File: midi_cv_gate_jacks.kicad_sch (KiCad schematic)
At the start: 32 parts, among them J10 CV_I, J11 CV_J, J12 CV_K, J13 CV_L, J14 CV_M, J15 CV_N, J16 CV_O, J17 CV_P, J18 GATE_A, J19 GATE_B, J2 CV_A, J20 GATE_C, J21 GATE_D, J22 GATE_E, J23 GATE_F, J24 GATE_G, J25 GATE_H, J26 GATE_I, J27 GATE_J, J28 GATE_K, J29 GATE_L, J3 CV_B, J30 GATE_M, J31 GATE_N, J32 GATE_O, J33 GATE_P, J4 CV_C, J5 CV_D, J6 CV_E, J7 CV_F, J8 CV_G, J9 CV_H

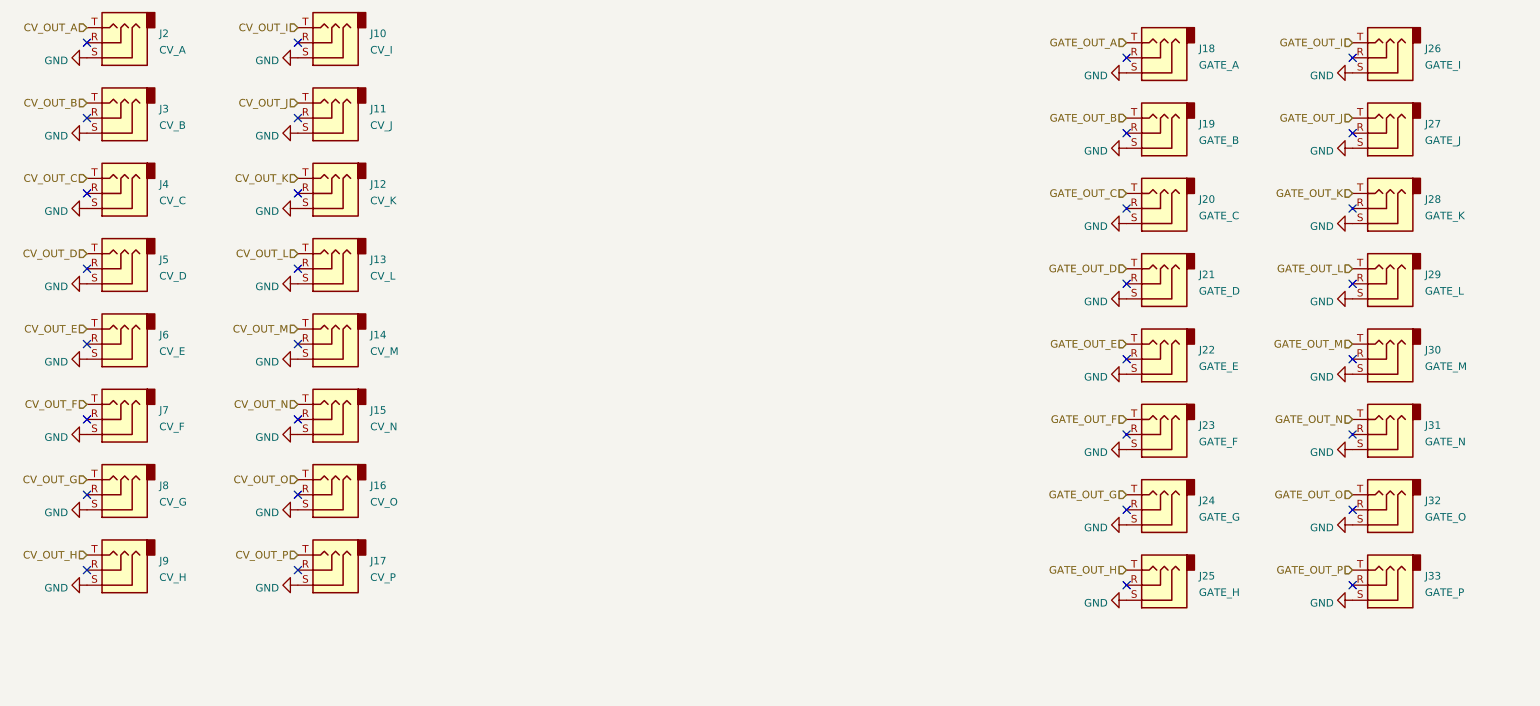
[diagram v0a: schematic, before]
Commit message: Replace soic-14 with dip 14 for DACs, add pulldowns on opamp inputs
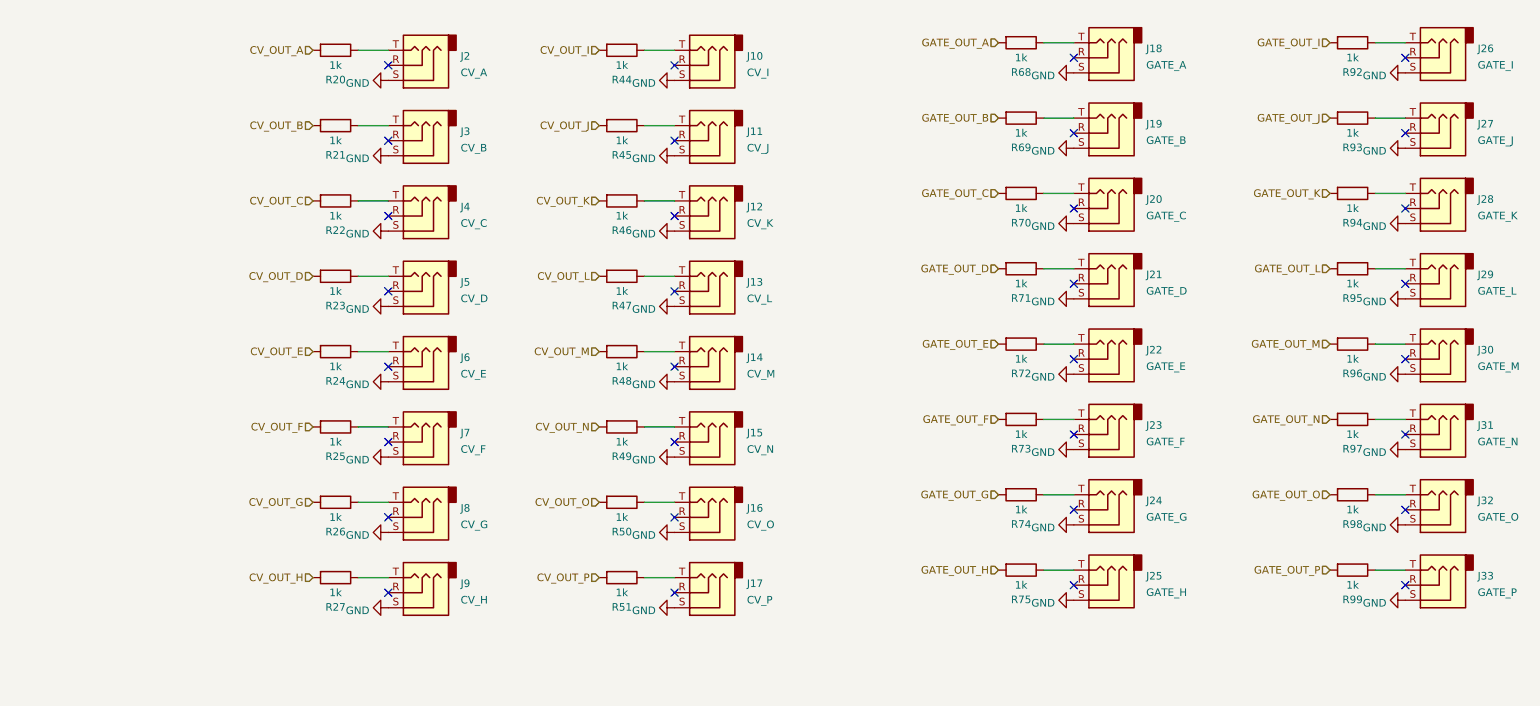
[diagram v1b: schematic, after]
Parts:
- added R20, R21, R22, R23, R24, R25, R26, R27, R44, R45, R46, R47, R48, R49, R50, R51, R68, R69, R70, R71, R72, R73, R74, R75, R92, R93, R94, R95, R96, R97, R98, R99: 1k, Resistor_SMD:R_1206_3216Metric_Pad1.30x1.75mm_HandSolder, symbol Device:R
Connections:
- net CV_OUT_A: now also R20.2; no longer J2.T
- net CV_OUT_B: now also R21.2; no longer J3.T
- net CV_OUT_C: now also R22.2; no longer J4.T
- net CV_OUT_D: now also R23.2; no longer J5.T
- net CV_OUT_E: now also R24.2; no longer J6.T
- net CV_OUT_F: now also R25.2; no longer J7.T
- net CV_OUT_G: now also R26.2; no longer J8.T
- net CV_OUT_H: now also R27.2; no longer J9.T
- net CV_OUT_I: now also R44.2; no longer J10.T
- net CV_OUT_J: now also R45.2; no longer J11.T
- net CV_OUT_K: now also R46.2; no longer J12.T
- net CV_OUT_L: now also R47.2; no longer J13.T
- net CV_OUT_M: now also R48.2; no longer J14.T
- net CV_OUT_N: now also R49.2; no longer J15.T
- net CV_OUT_O: now also R50.2; no longer J16.T
- net CV_OUT_P: now also R51.2; no longer J17.T
- net GATE_OUT_A: now also R68.2; no longer J18.T
- net GATE_OUT_B: now also R69.2; no longer J19.T
- net GATE_OUT_C: now also R70.2; no longer J20.T
- net GATE_OUT_D: now also R71.2; no longer J21.T
- net GATE_OUT_E: now also R72.2; no longer J22.T
- net GATE_OUT_F: now also R73.2; no longer J23.T
- net GATE_OUT_G: now also R74.2; no longer J24.T
- net GATE_OUT_H: now also R75.2; no longer J25.T
- net GATE_OUT_I: now also R92.2; no longer J26.T
- net GATE_OUT_J: now also R93.2; no longer J27.T
- net GATE_OUT_K: now also R94.2; no longer J28.T
- net GATE_OUT_L: now also R95.2; no longer J29.T
- net GATE_OUT_M: now also R96.2; no longer J30.T
- net GATE_OUT_N: now also R97.2; no longer J31.T
- net GATE_OUT_O: now also R98.2; no longer J32.T
- net GATE_OUT_P: now also R99.2; no longer J33.T
- new net: J20.T, R70.1
- new net: J3.T, R21.1
- new net: J13.T, R47.1
- new net: J27.T, R93.1
- new net: J26.T, R92.1
- new net: J16.T, R50.1
- new net: J4.T, R22.1
- new net: J17.T, R51.1
- new net: J5.T, R23.1
- new net: J24.T, R74.1
- new net: J14.T, R48.1
- new net: J25.T, R75.1
- new net: J29.T, R95.1
- new net: J18.T, R68.1
- new net: J15.T, R49.1
- new net: J31.T, R97.1
- new net: J10.T, R44.1
- new net: J19.T, R69.1
- new net: J7.T, R25.1
- new net: J33.T, R99.1
- new net: J21.T, R71.1
- new net: J8.T, R26.1
- new net: J23.T, R73.1
- new net: J30.T, R96.1
- new net: J12.T, R46.1
- new net: J6.T, R24.1
- new net: J32.T, R98.1
- new net: J11.T, R45.1
- new net: J2.T, R20.1
- new net: J9.T, R27.1
- new net: J28.T, R94.1
- new net: J22.T, R72.1
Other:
- moved on the sheet: J10, J11, J12, J13, J14, J15, J16, J17, J18, J19, J2, J20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

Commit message: Fixed alignment of jacks and LEDs
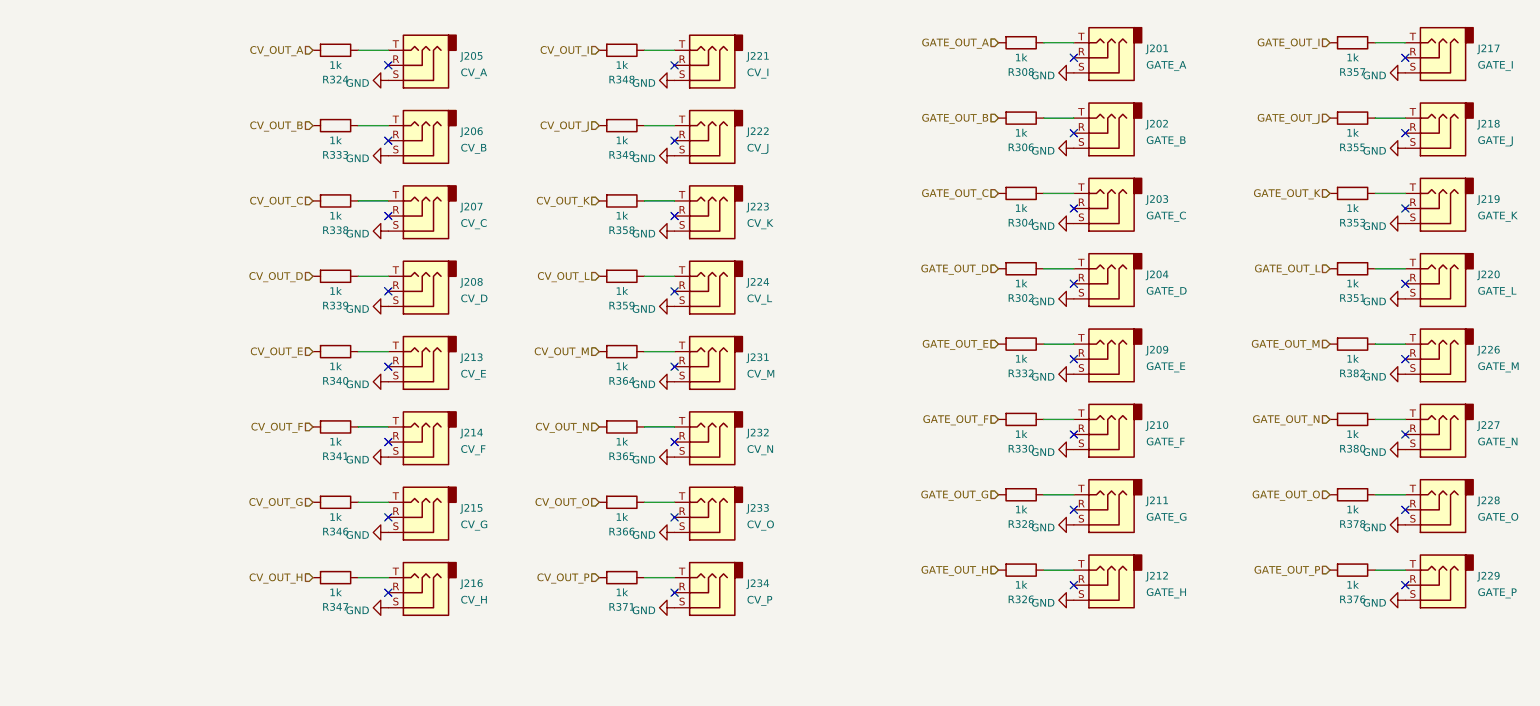
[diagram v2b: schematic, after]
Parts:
- renumbered J18 to J201, J19 to J202, J20 to J203, J21 to J204, J2 to J205, J3 to J206, J4 to J207, J5 to J208, J22 to J209, J23 to J210, J24 to J211, J25 to J212, J6 to J213, J7 to J214, J8 to J215, J9 to J216, J26 to J217, J27 to J218, J28 to J219, J29 to J220, J10 to J221, J11 to J222, J12 to J223, J13 to J224, J30 to J226, J31 to J227, J32 to J228, J33 to J229, J14 to J231, J15 to J232, J16 to J233, J17 to J234, R71 to R302, R70 to R304, R69 to R306, R68 to R308, R20 to R324, R75 to R326, R74 to R328, R73 to R330, R72 to R332, R21 to R333, R22 to R338, R23 to R339, R24 to R340, R25 to R341, R26 to R346, R27 to R347, R44 to R348, R45 to R349, R95 to R351, R94 to R353, R93 to R355, R92 to R357, R46 to R358, R47 to R359, R48 to R364, R49 to R365, R50 to R366, R51 to R371, R99 to R376, R98 to R378, R97 to R380, R96 to R382

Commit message: Cleanups and title blocks
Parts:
- renumbered R326 to R325, R328 to R327, R330 to R329, R332 to R331, R324 to R332, R371 to R367
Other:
- company: (none) -> RobotDialogs
- title: (none) -> Eurorack MIDI 16x16 CV Gate
- moved on the sheet: J201, J202, J203, J204, J205, J206, J207, J208, J209, J210, J211, J212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
